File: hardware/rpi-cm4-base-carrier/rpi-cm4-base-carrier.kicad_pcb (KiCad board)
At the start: 4 copper layers, 169 x 134.1 mm, 149 parts, among them IC1 KTD2052BEVAA-TR, IC2 LM74610QDGKRQ1, IC3 LM74610QDGKRQ1, IC4 LM74610QDGKRQ1, IC5 LMR51450FNDRRR, J1 690-019-298-412, J10 Conn_02x05_Odd_Even, J11 XM7B-0442, J12 USB4105-GF-A, J13 1190297, J2 ERM8-040-01-X-D-EM2-L-XX, J3 PJ-102BH, J4 USB4105-GF-A, J5 THD-02-R, J6 JT4-1202HL, J7 Micro_SD_Card_Det, J8 Conn_02x10_Odd_Even, J9 690-008-221-904, Q1 STL6P3LLH6, Q2 STL6P3LLH6, Q3 STL11N3LLH6, Q4 STL11N3LLH6, Q5 STL11N3LLH6, U1 RT9742SNGV, U2 74LVC1G07SE-7, U3 STUSB4500QTR, U4 RT9742GGJ5, U5 FSUSB42MUX, U6 USB2514B-I/M2, U7 STUSB4500QTR, U8 AP22653W6, U9 74LVC1G07SE-7, Y1 CX3225CA24000D0HSSCC

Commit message: layout ready for review as major components now complete
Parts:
- removed R8: nf, Resistor_SMD:R_0402_1005Metric
- moved Q5 168.7 mm to (187.3, 58.3), turned to -90 degrees
- moved J13 165.7 mm to (186.7, 44.0), turned to -90 degrees
- moved C46 147.8 mm to (178.3, 54.9), turned to 180 degrees
- moved C44 146.5 mm to (179.6, 58.2), turned to -90 degrees
- moved C45 144.9 mm to (177.1, 58.2), turned to -90 degrees
- moved IC4 144.4 mm to (183.1, 58.2), turned to -90 degrees
- moved J3 141.4 mm to (164.6, 146.2), turned to 180 degrees
- moved J8 136.5 mm to (115.9, 45.6)
- moved U2 95.8 mm to (124.3, 59.9)
- moved C47 64.8 mm to (159.8, 69.5)
- moved C48 64.8 mm to (168.5, 68.5)
- moved C49 64.8 mm to (157.3, 63.0)
- moved C50 64.8 mm to (157.3, 60.2)
- moved IC5 64.8 mm to (164.2, 66.2)
- moved L1 64.8 mm to (164.2, 60.2)
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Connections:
- net Net-(IC4-ANODE) renamed /Power_Input/AUX_20V
- J7 pad 9: Net-(J7-DET_B) -> unconnected-(J7-DET_B-Pad9)
- Module1 pad 76: /SDCard/Reserved -> /CM4 GPIO/Reserved
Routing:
- net /CM4 GPIO/SD_PWR_ON: track 4.91 -> 96.5 mm, vias 0 -> 2
- net /CM4 High Speed/HDMI0_HOTPLUG: track 0.00 -> 58.0 mm, vias 0 -> 2
- net +5V: track 30.6 -> 83.2 mm, vias 3 -> 13
- net /CM4 High Speed/HDMI0_SDA: track 0.00 -> 48.7 mm, vias 0 -> 2
- net /CM4 High Speed/HDMI0_SCL: track 0.00 -> 45.4 mm, vias 0 -> 2
- net GND: track 221.7 -> 260.7 mm, vias 118 -> 149
- net /CM4 High Speed/USB_OTG_ID: track 4.62 -> 27.5 mm, vias 0 -> 2
- net /CM4 High Speed/HDMI/HDMI_5v: track 3.86 -> 18.9 mm
- net /Power_Input/USBC_PWR.Sheet/+2V7: track 7.41 -> 21.7 mm, vias 1 -> 2
- net /Power_Input/USBC_PWR.Sheet1/+2V7: track 10.9 -> 25.1 mm
- net Net-(IC4-GATE_DRIVE): track 0.00 -> 11.2 mm
- net /CM4 GPIO/SD_CLK: track 67.9 -> 78.1 mm, vias 2 -> 0
- net Net-(IC4-VCAPH): track 0.00 -> 9.01 mm
- net /CM4 GPIO/SD_DAT2: track 66.6 -> 75.2 mm
- net Net-(IC4-VCAPL): track 0.00 -> 8.21 mm
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- added copper zone on In2.Cu, net +20V
- added copper zone on F.Cu, net +5V
- added copper zone on F.Cu, net /Power_Input/AUX_20V
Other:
- board size 169 x 134.1 mm -> 110 x 117 mm

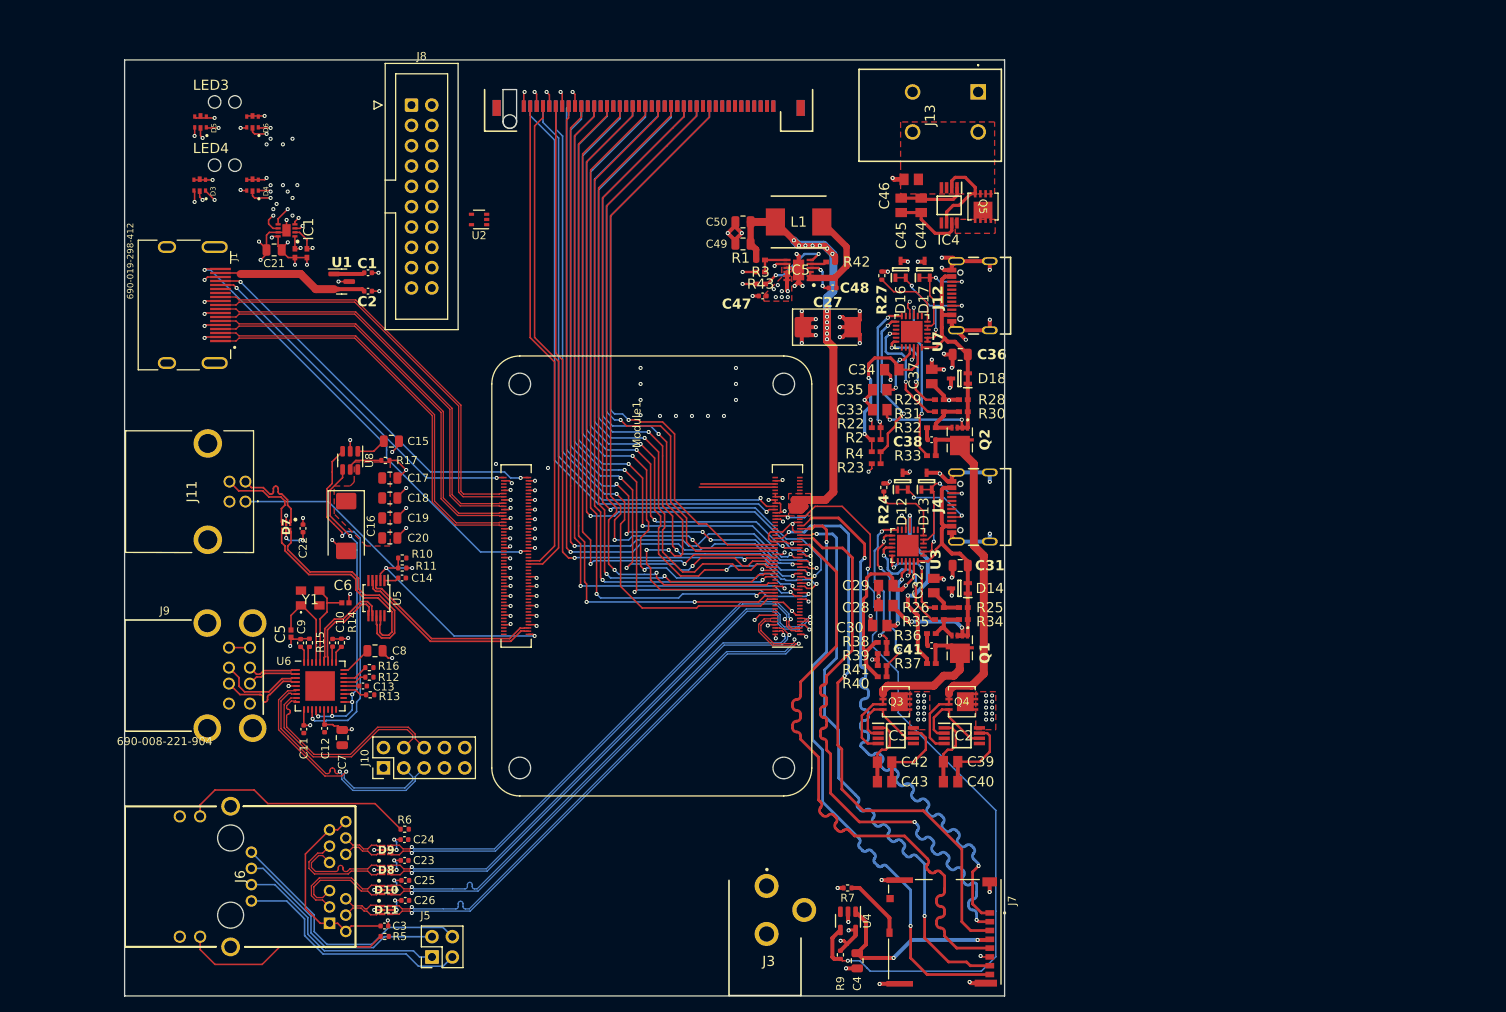
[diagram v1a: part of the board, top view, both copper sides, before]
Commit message: good routing and power plane progress, just some final plane progress remaining
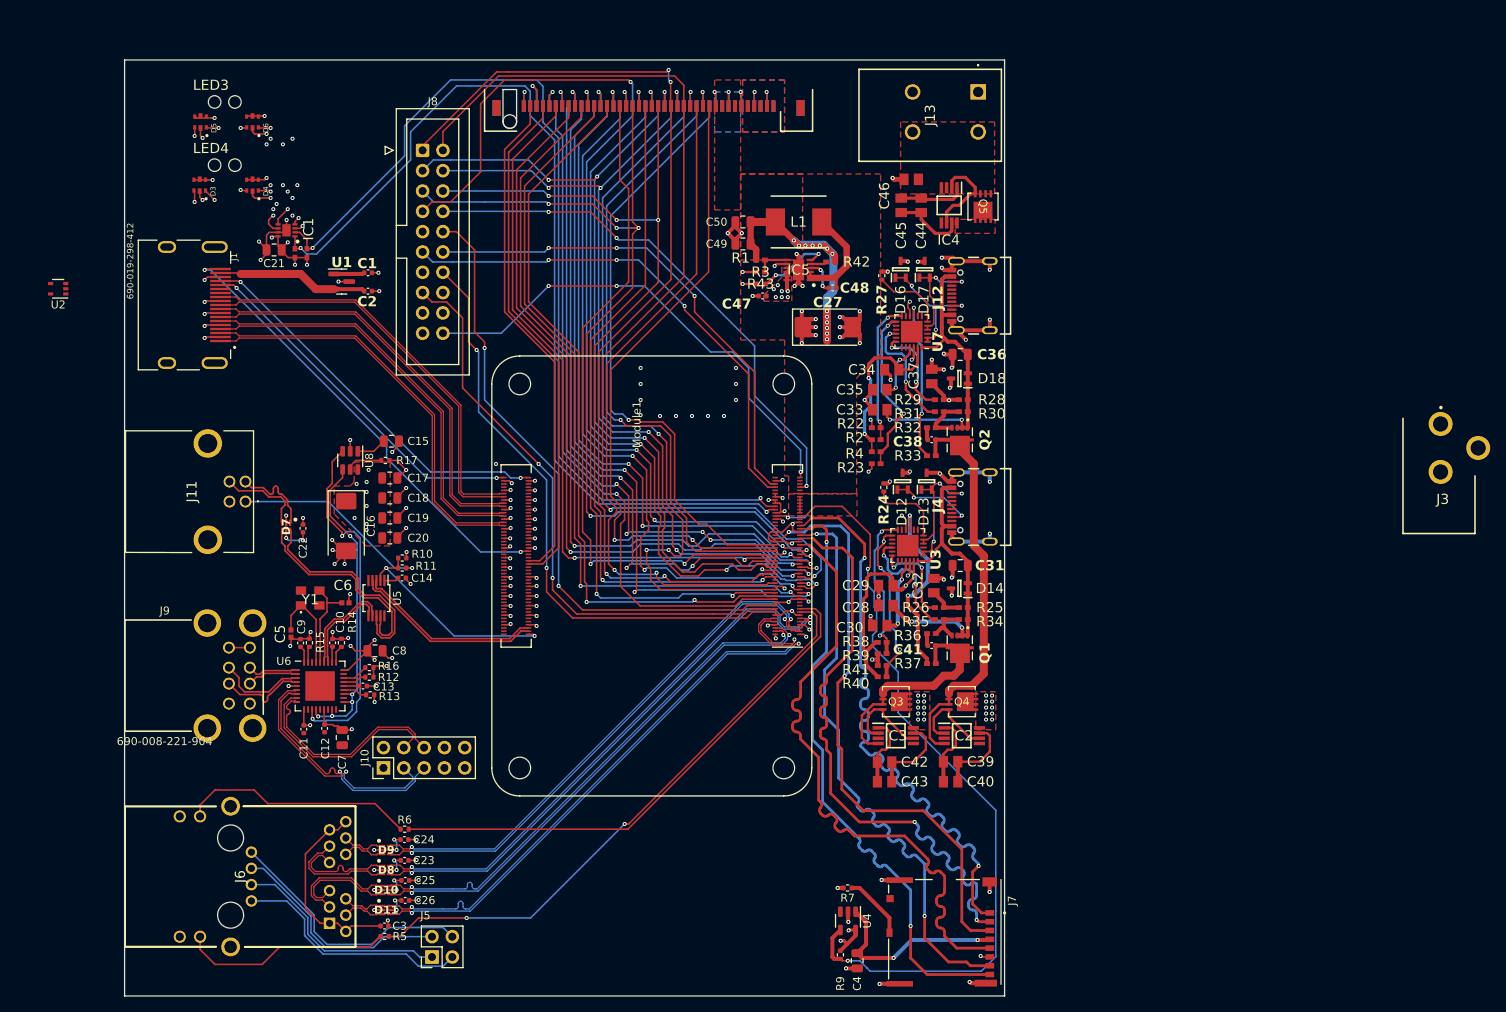
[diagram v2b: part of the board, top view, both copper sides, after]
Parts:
- moved J3 102.1 mm to (248.8, 88.5)
- moved U2 53.3 mm to (71.7, 68.6)
- moved J8 5.83 mm to (117.2, 51.3)
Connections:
- J2 pad 16: unconnected-(J2-Pad16) -> /Board_Edge_Connector/GPIO25
- J2 pad 28: unconnected-(J2-Pad28) -> /Board_Edge_Connector/GPIO19
- J2 pad 36: unconnected-(J2-Pad36) -> /Board_Edge_Connector/GPIO15
- J2 pad 63: +20V -> +3V3
- J2 pad 64: +20V -> +5V
- J2 pad 67: +20V -> +3V3
- J2 pad 68: +20V -> +5V
- J2 pad 75: +3V3 -> +20V
- J2 pad 76: +5V -> +20V
- J2 pad 79: +3V3 -> +20V
- J2 pad 80: +5V -> +20V
- J8 pad 5: GND -> /Board_Edge_Connector/GPIO15
- Module1 pad 26: GND -> /Board_Edge_Connector/GPIO19
- Module1 pad 41: GND -> /Board_Edge_Connector/GPIO25
- Module1 pad 51: GND -> /Board_Edge_Connector/GPIO15
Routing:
- net /Board_Edge_Connector/GPIO15: track 0.00 -> 115.6 mm, vias 0 -> 5
- net /Board_Edge_Connector/GPIO25: track 0.00 -> 94.8 mm, vias 0 -> 2
- net /Board_Edge_Connector/GPIO19: track 0.00 -> 93.1 mm, vias 0 -> 2
- net unconnected-(J2-Pad16): track 89.6 -> 0.00 mm, vias 2 -> 0
- net unconnected-(J2-Pad28): track 87.8 -> 0.00 mm, vias 2 -> 0
- net unconnected-(J2-Pad36): track 85.3 -> 0.00 mm, vias 2 -> 0
- net GND: track 260.7 -> 345.3 mm, vias 149 -> 177
- net /Board_Edge_Connector/EEPROM_nWP: track 0.00 -> 79.8 mm, vias 0 -> 2
- net /Board_Edge_Connector/SYNC_IN: track 0.00 -> 75.6 mm, vias 0 -> 2
- net /Board_Edge_Connector/SYNC_OUT: track 0.00 -> 74.3 mm, vias 0 -> 2
- net /CM4 GPIO/ETH_LEDY: track 0.00 -> 73.8 mm, vias 0 -> 2
- net /CM4 GPIO/ETH_LEDG: track 0.00 -> 67.1 mm
- net /Board_Edge_Connector/nRPIBOOT: track 0.00 -> 67.0 mm, vias 0 -> 3
- net /Board_Edge_Connector/GLOBAL_EN: track 0.00 -> 61.3 mm, vias 0 -> 3
- net /Board_Edge_Connector/AIN0: track 9.51 -> 63.6 mm, vias 0 -> 3
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- added copper zone on B.Cu, net +20V
- added copper zone on B.Cu, net +3V3
- added copper zone on In2.Cu, net /CM4 High Speed/USB2-HUB/VBUS
